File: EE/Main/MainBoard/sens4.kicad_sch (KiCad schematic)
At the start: 3 parts, among them J5 Conn_02x13_Odd_Even

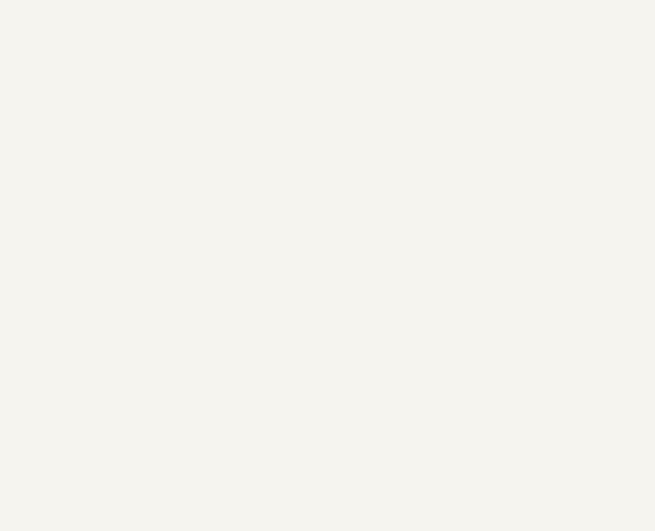
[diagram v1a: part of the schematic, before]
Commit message: WIP - Moving Sensor to IO Expander
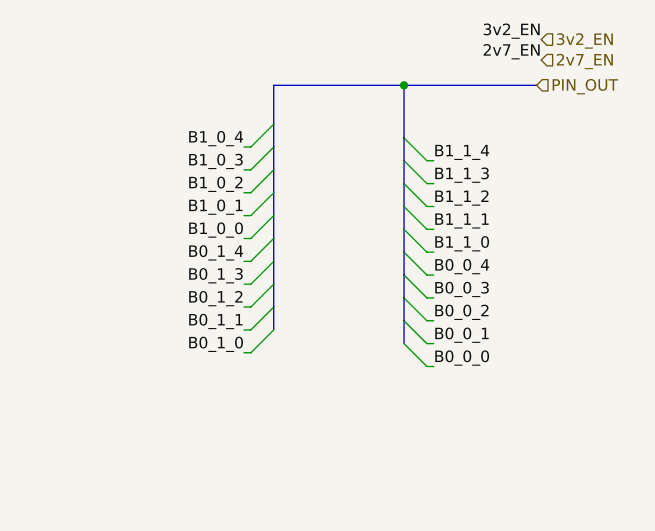
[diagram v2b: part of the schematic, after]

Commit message: Updated layout, and placement for main board
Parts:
- removed J5: Conn_02x13_Odd_Even, Connector_PinHeader_1.27mm:PinHeader_2x13_P1.27mm_Vertical_SMD, symbol Connector_Generic:Conn_02x13_Odd_Even
- added J5: Conn_01x04_Male, Connector_PinSocket_2.54mm:PinSocket_1x04_P2.54mm_Vertical, symbol Connector:Conn_01x04_Male
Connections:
- net GND: now also J5.4 (Pin_4)
- net VCC: now also J5.1 (Pin_1)
- new net SCL: J5.2 (Pin_2)
- new net SDA: J5.3 (Pin_3)
- no-connect marks 2 -> 0

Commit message: Routine Update
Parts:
- H10, H9: footprint MountingHole:MountingHole_2.5mm -> MountingHole:MountingHole_2.7mm
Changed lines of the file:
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@@
       (effects (font (size 1.27 1.27)) (justify left))
     )
-    (property "Footprint" "MountingHole:MountingHole_2.5mm" (id 2) (at 130.81 78.486 0)
+    (property "Footprint" "MountingHole:MountingHole_2.7mm" (id 2) (at 130.81 78.486 0)
       (effects (font (size 1.27 1.27)) hide)
     )
@@
       (effects (font (size 1.27 1.27)) (justify left))
     )
-    (property "Footprint" "MountingHole:MountingHole_2.5mm" (id 2) (at 130.81 122.682 0)
+    (property "Footprint" "MountingHole:MountingHole_2.7mm" (id 2) (at 130.81 122.682 0)
       (effects (font (size 1.27 1.27)) hide)
     )
